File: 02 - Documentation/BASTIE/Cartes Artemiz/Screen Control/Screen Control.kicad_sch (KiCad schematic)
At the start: 1 part, among them U1 Teensy3.5

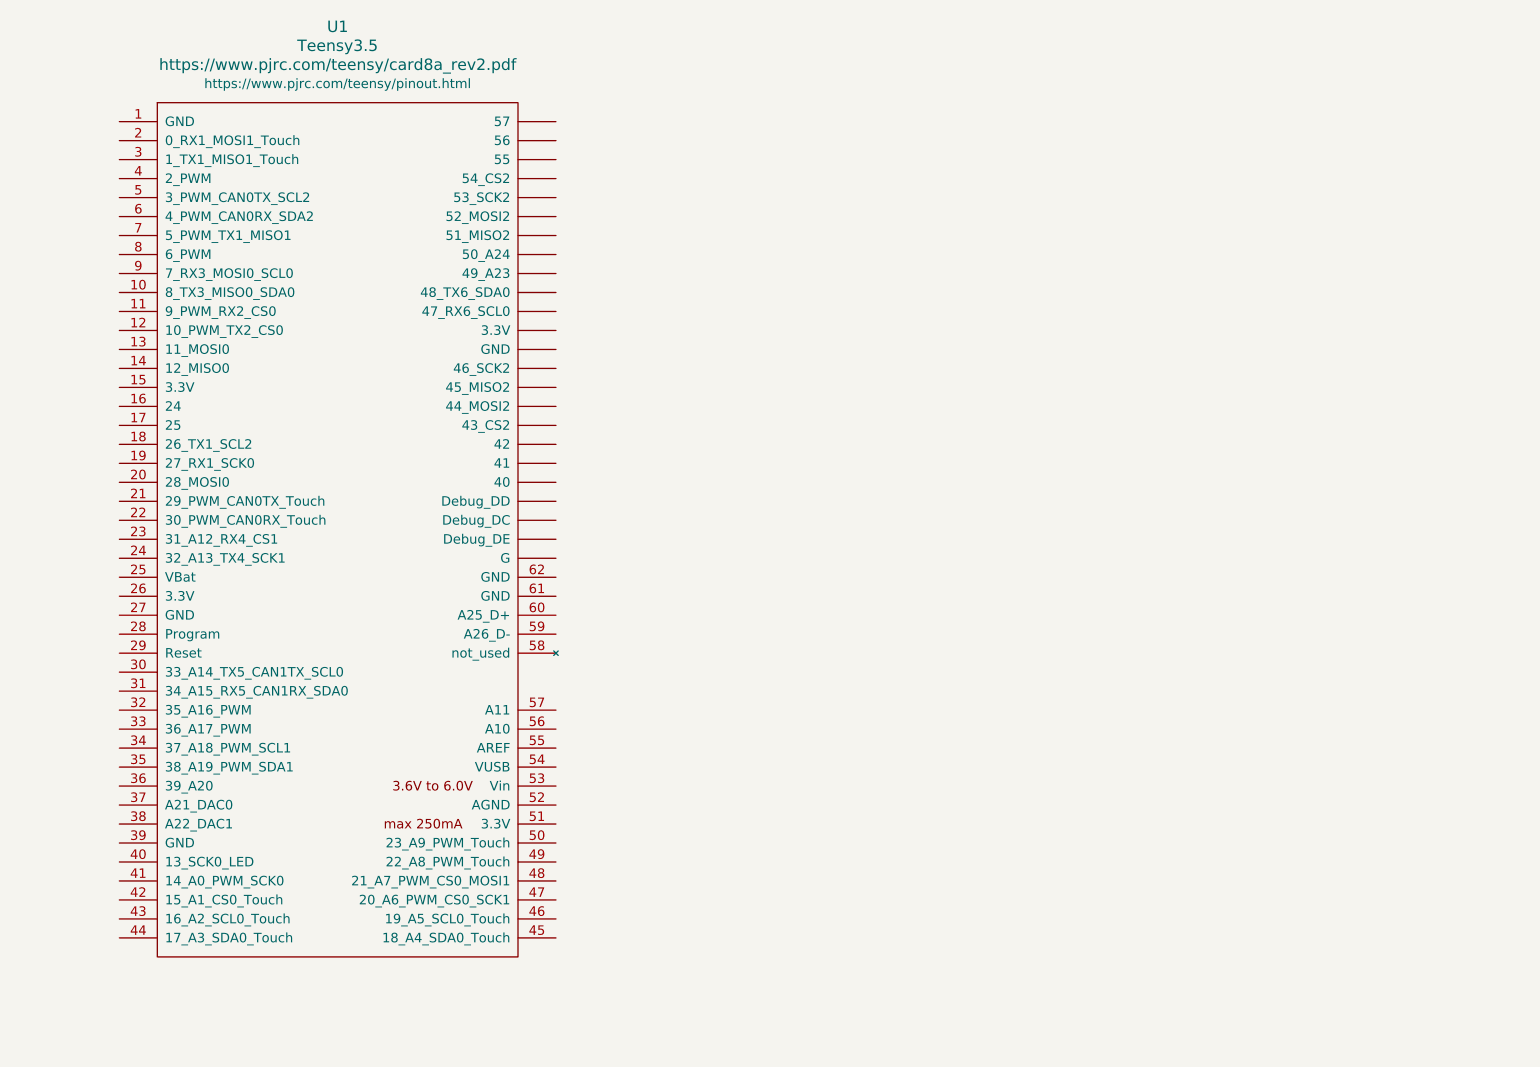
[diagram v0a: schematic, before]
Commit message: Librairie Kicad+ DSB Controller
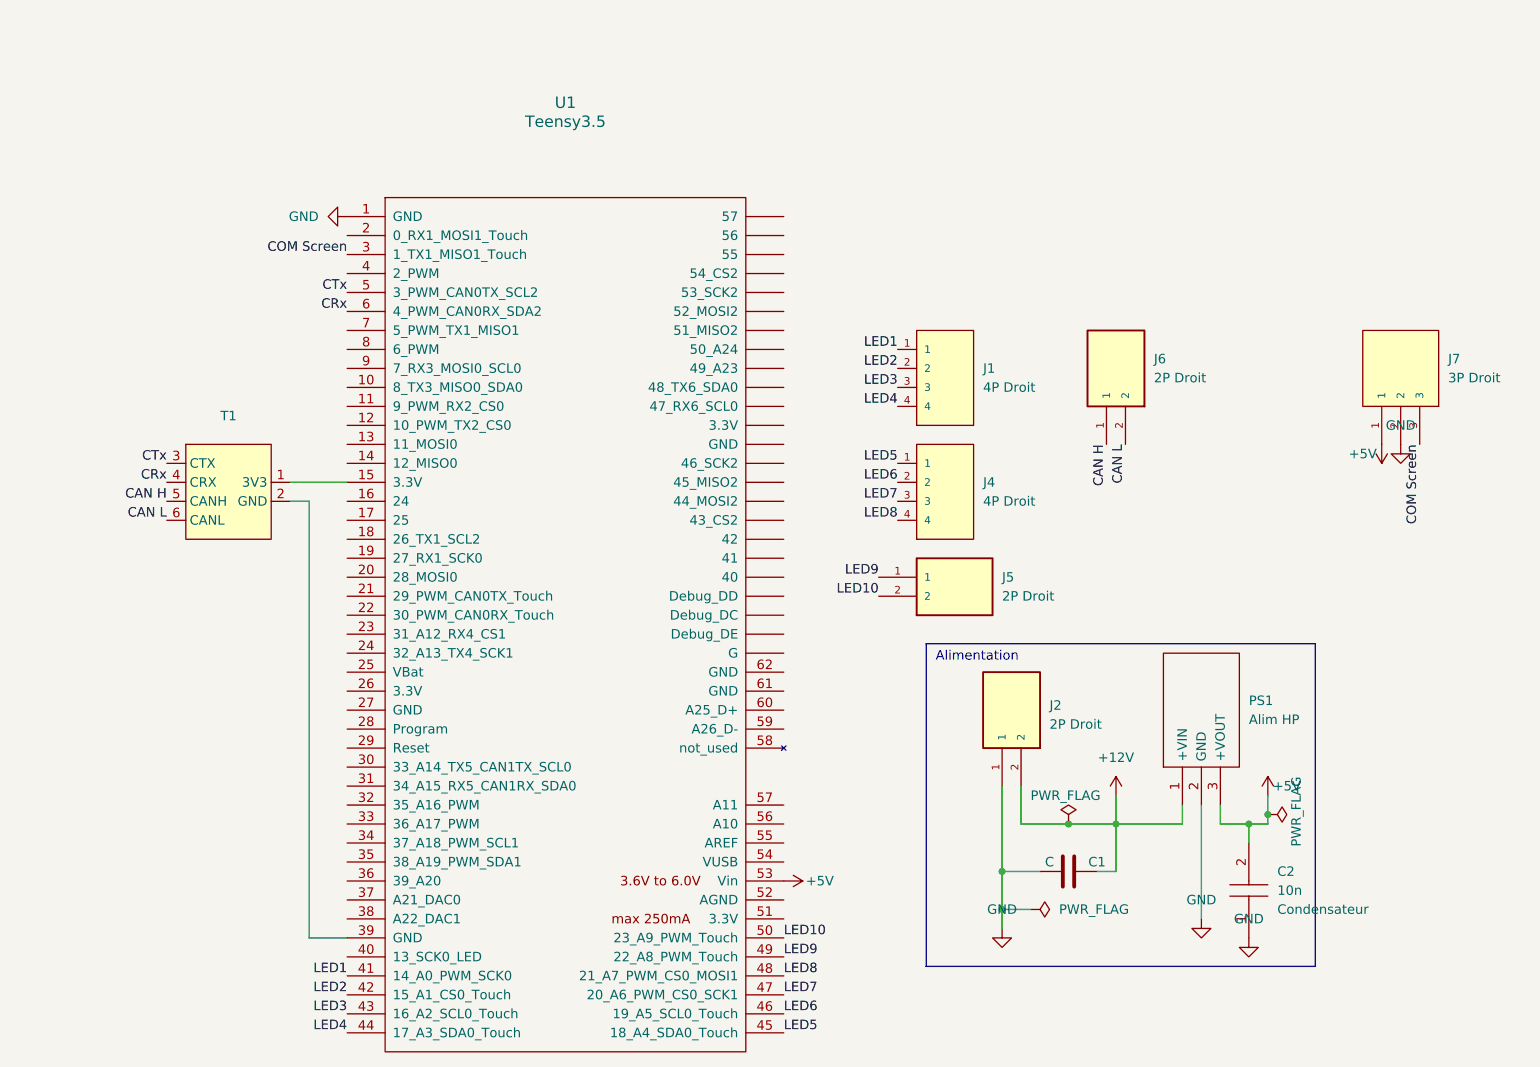
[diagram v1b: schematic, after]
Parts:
- removed U1: Teensy3.5, symbol EPSA_lib:Teensy3.5
- added C1: C, Capacitor_THT:CP_Radial_D5.0mm_P2.00mm, symbol Device:C
- added C2: 10n, EPSA_lib:CAPC2012X130N, symbol EPSA_lib:Condensateur 0805Y1000104JXT
- added J1, J4: 4P Droit 22-11-2042, EPSA_lib:MOLEX_22-11-2042, symbol EPSA_Lib:4P Droit 22-11-2042
- added J2, J5, J6: 2P Droit 2-11-2022, EPSA_lib:MOLEX_22-11-2022, symbol EPSA_lib:2P Droit 2-11-2022
- added J7: 3P Droit 22-11-2032, EPSA_lib:MOLEX_22-11-2032, symbol EPSA_Lib:3P Droit 22-11-2032
- added PS1: Alim HP TSR_2-2450, EPSA_lib:TSR-2, symbol EPSA_Lib:Alim HP TSR_2-2450
- added T1: ~, EPSA_lib:CAN_Transceiver, symbol EPSA_Lib:CAN Transceiver
- added U1: Teensy3.5, EPSA_lib:Teensy35_36, symbol EPSA_Lib:Teensy3.5
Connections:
- new net: T1.1 (3V3), U1.15 (3.3V)
- new net: T1.2 (GND), U1.39 (GND)
- new net +12V: C1.2, J2.2, PS1.1 (+VIN)
- new net +5V: C2.2, J7.1, PS1.3 (+VOUT), U1.53 (Vin)
- new net CAN H: J6.1, T1.5 (CANH)
- new net CAN L: J6.2, T1.6 (CANL)
- new net COM Screen: J7.3, U1.3 (1_TX1_MISO1_Touch)
- new net CRx: T1.4 (CRX), U1.6 (4_PWM_CAN0RX_SDA2)
- new net CTx: T1.3 (CTX), U1.5 (3_PWM_CAN0TX_SCL2)
- new net GND: C1.1, C2.1, J2.1, J7.2, PS1.2 (GND), U1.1 (GND)
- new net LED1: J1.1, U1.41 (14_A0_PWM_SCK0)
- new net LED10: J5.2, U1.50 (23_A9_PWM_Touch)
- new net LED2: J1.2, U1.42 (15_A1_CS0_Touch)
- new net LED3: J1.3, U1.43 (16_A2_SCL0_Touch)
- new net LED4: J1.4, U1.44 (17_A3_SDA0_Touch)
- new net LED5: J4.1, U1.45 (18_A4_SDA0_Touch)
- new net LED6: J4.2, U1.46 (19_A5_SCL0_Touch)
- new net LED7: J4.3, U1.47 (20_A6_PWM_CS0_SCK1)
- new net LED8: J4.4, U1.48 (21_A7_PWM_CS0_MOSI1)
- new net LED9: J5.1, U1.49 (22_A8_PWM_Touch)
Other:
- note added: "Alimentation"

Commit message: Corrections mineures
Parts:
- added C3: 1u, EPSA_lib:CAPC2012X130N, symbol EPSA_lib:Condensateur 0805Y1000104JXT
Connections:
- net at T1.1 (3V3), U1.15 (3.3V): now also C3.2
- net at T1.2 (GND), U1.39 (GND): now also C3.1
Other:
- moved on the sheet: T1

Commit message: Kicadlib + Modifs cartes
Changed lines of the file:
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@@
 	(wire
 		(pts
-			(xy 50.8 88.9) (xy 63.5 88.9)
+			(xy 50.8 88.9) (xy 43.18 88.9)
 		)
 		(stroke
@@
 	(wire
 		(pts
-			(xy 50.8 86.36) (xy 63.5 86.36)
+			(xy 50.8 86.36) (xy 43.18 86.36)
 		)
 		(stroke
@@
 	(wire
 		(pts
-			(xy 50.8 83.82) (xy 63.5 83.82)
+			(xy 50.8 83.82) (xy 43.18 83.82)
 		)
 		(stroke
@@
 	(wire
 		(pts
-			(xy 50.8 81.28) (xy 63.5 81.28)
+			(xy 50.8 81.28) (xy 43.18 81.28)
 		)
 		(stroke
@@
 	)
 	(label "CAN L"
-		(at 63.5 88.9 180)
-		(fields_autoplaced yes)
-		(effects
-			(font
-				(size 1.27 1.27)
-			)
-			(justify right bottom)
+		(at 43.18 88.9 0)
+		(fields_autoplaced yes)
+		(effects
+			(font
+				(size 1.27 1.27)
+			)
+			(justify left bottom)
 		)
 	)
@@
 	)
 	(label "CRx"
-		(at 63.5 83.82 180)
-		(fields_autoplaced yes)
-		(effects
-			(font
-				(size 1.27 1.27)
-			)
-			(justify right bottom)
+		(at 43.18 83.82 0)
+		(fields_autoplaced yes)
+		(effects
+			(font
+				(size 1.27 1.27)
+			)
+			(justify left bottom)
 		)
 	)
@@
 	)
 	(label "CTx"
-		(at 63.5 81.28 180)
-		(fields_autoplaced yes)
-		(effects
-			(font
-				(size 1.27 1.27)
-			)
-			(justify right bottom)
+		(at 43.18 81.28 0)
+		(fields_autoplaced yes)
+		(effects
+			(font
+				(size 1.27 1.27)
+			)
+			(justify left bottom)
 		)
 	)
@@
 	)
 	(label "CAN H"
-		(at 63.5 86.36 180)
-		(fields_autoplaced yes)
-		(effects
-			(font
-				(size 1.27 1.27)
-			)
-			(justify right bottom)
-		)
-	)
+		(at 43.18 86.36 0)
+		(fields_autoplaced yes)
+		(effects
+			(font
+				(size 1.27 1.27)
+			)
+			(justify left bottom)
+		)
+	)
